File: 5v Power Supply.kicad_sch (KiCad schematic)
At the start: 15 parts, among them J15 Conn_01x02_Pin, J5 Screw_Terminal_01x02, U1 TPS56528DDA

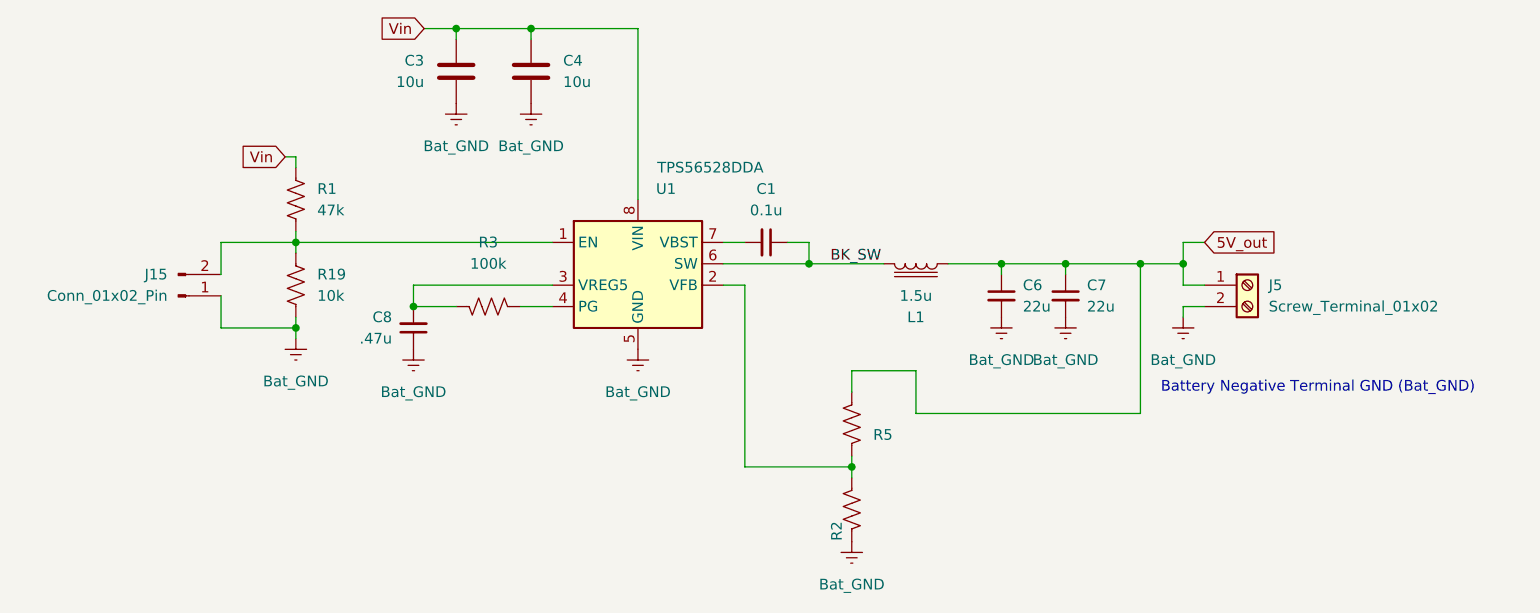
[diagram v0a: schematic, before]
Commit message: Simplified Schematic and finished PCB
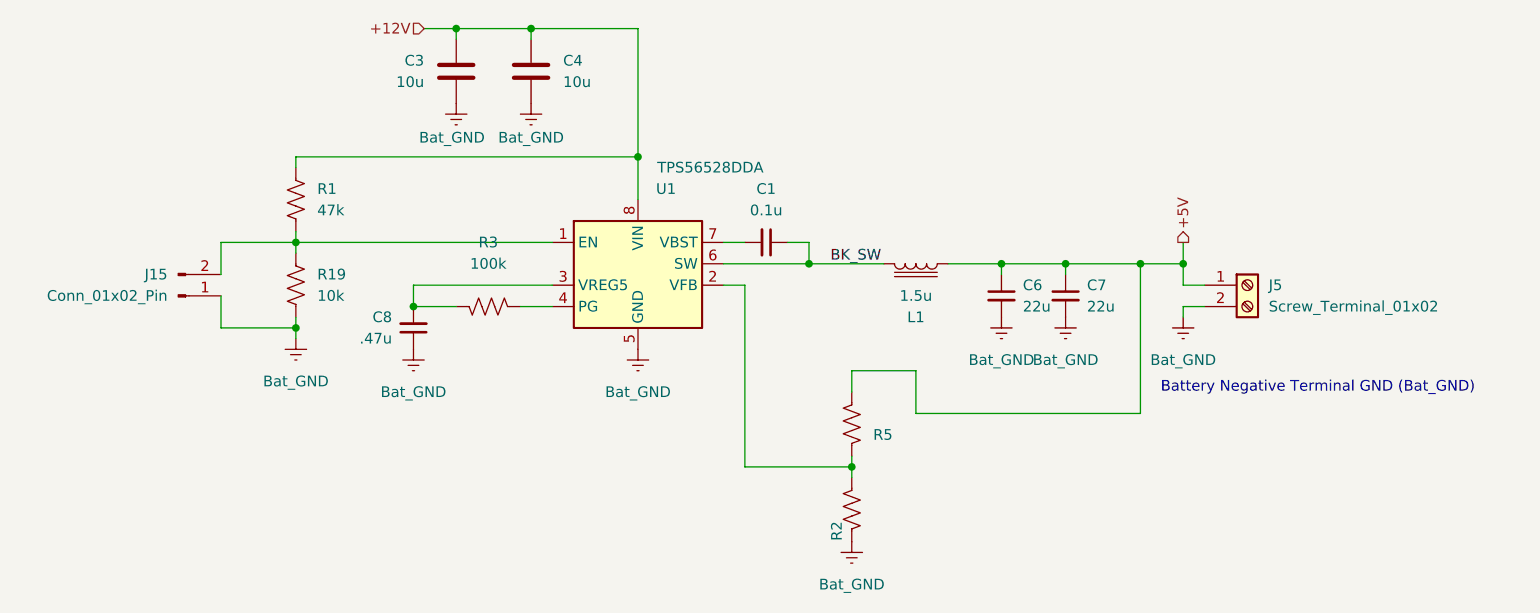
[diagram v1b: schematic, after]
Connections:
- net 5V_out renamed +5V
- net Vin renamed +12V
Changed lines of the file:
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@@
+	)
+	(junction
+		(at 140.97 77.47)
+		(diameter 0)
+		(color 0 0 0 0)
 	)
 	(junction
@@
 	(wire
 		(pts
-			(xy 140.97 82.55) (xy 140.97 62.23)
+			(xy 140.97 82.55) (xy 140.97 77.47)
 		)
 		(stroke
@@
 	(wire
 		(pts
+			(xy 140.97 77.47) (xy 140.97 62.23)
+		)
+		(stroke
+			(width 0)
+			(type default)
+		)
+	)
+	(wire
+		(pts
 			(xy 128.27 62.23) (xy 128.27 63.5)
 		)
@@
 	(wire
 		(pts
-			(xy 99.06 77.47) (xy 100.33 77.47)
-		)
-		(stroke
-			(width 0)
-			(type default)
-		)
-	)
-	(wire
-		(pts
 			(xy 166.37 114.3) (xy 153.67 114.3)
 		)
@@
 	(wire
 		(pts
-			(xy 205.74 87.63) (xy 208.28 87.63)
-		)
-		(stroke
-			(width 0)
-			(type default)
-		)
-	)
-	(wire
-		(pts
 			(xy 130.81 92.71) (xy 114.3 92.71)
 		)
@@
 		(pts
 			(xy 166.37 113.03) (xy 166.37 114.3)
+		)
+		(stroke
+			(width 0)
+			(type default)
+		)
+	)
+	(wire
+		(pts
+			(xy 100.33 77.47) (xy 140.97 77.47)
 		)
 		(stroke
@@
 		)
 	)
-	(global_label "5V_out"
+	(hierarchical_label "+12V"
 		(shape input)
-		(at 208.28 87.63 0)
-		(fields_autoplaced yes)
+		(at 115.57 62.23 180)
 		(effects
 			(font
 				(size 1.27 1.27)
 			)
-			(justify left)
-		)
-		(property "Intersheetrefs" "${INTERSHEET_REFS}"
-			(at 217.5546 87.63 0)
-			(effects
-				(font
-					(size 1.27 1.27)
-				)
-				(justify left)
-				(hide yes)
-			)
-		)
-	)
-	(global_label "Vin"
-		(shape input)
-		(at 115.57 62.23 180)
-		(fields_autoplaced yes)
+			(justify right)
+		)
+	)
+	(hierarchical_label "+5V"
+		(shape output)
+		(at 205.74 87.63 90)
 		(effects
 			(font
 				(size 1.27 1.27)
 			)
-			(justify right)
-		)
-		(property "Intersheetrefs" "${INTERSHEET_REFS}"
-			(at 109.7424 62.23 0)
-			(effects
-				(font
-					(size 1.27 1.27)
-				)
-				(justify right)
-				(hide yes)
-			)
-		)
-	)
-	(global_label "Vin"
-		(shape input)
-		(at 99.06 77.47 180)
-		(fields_autoplaced yes)
-		(effects
-			(font
-				(size 1.27 1.27)
-			)
-			(justify right)
-		)
-		(property "Intersheetrefs" "${INTERSHEET_REFS}"
-			(at 93.2324 77.47 0)
-			(effects
-				(font
-					(size 1.27 1.27)
-				)
-				(justify right)
-				(hide yes)
-			)
+			(justify left)
 		)
 	)
@@
 		)
 		(property "Value" "Bat_GND"
-			(at 128.27 76.2 0)
+			(at 128.27 75.184 0)
 			(effects
 				(font
@@
 		)
 		(property "Value" "Bat_GND"
-			(at 119.38 76.2 0)
-			(effects
-				(font
+			(at 118.872 75.184 0)
+			(effects
+				(font

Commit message: Added bypass caps for 5V output and battery to protect from in rush and back emf
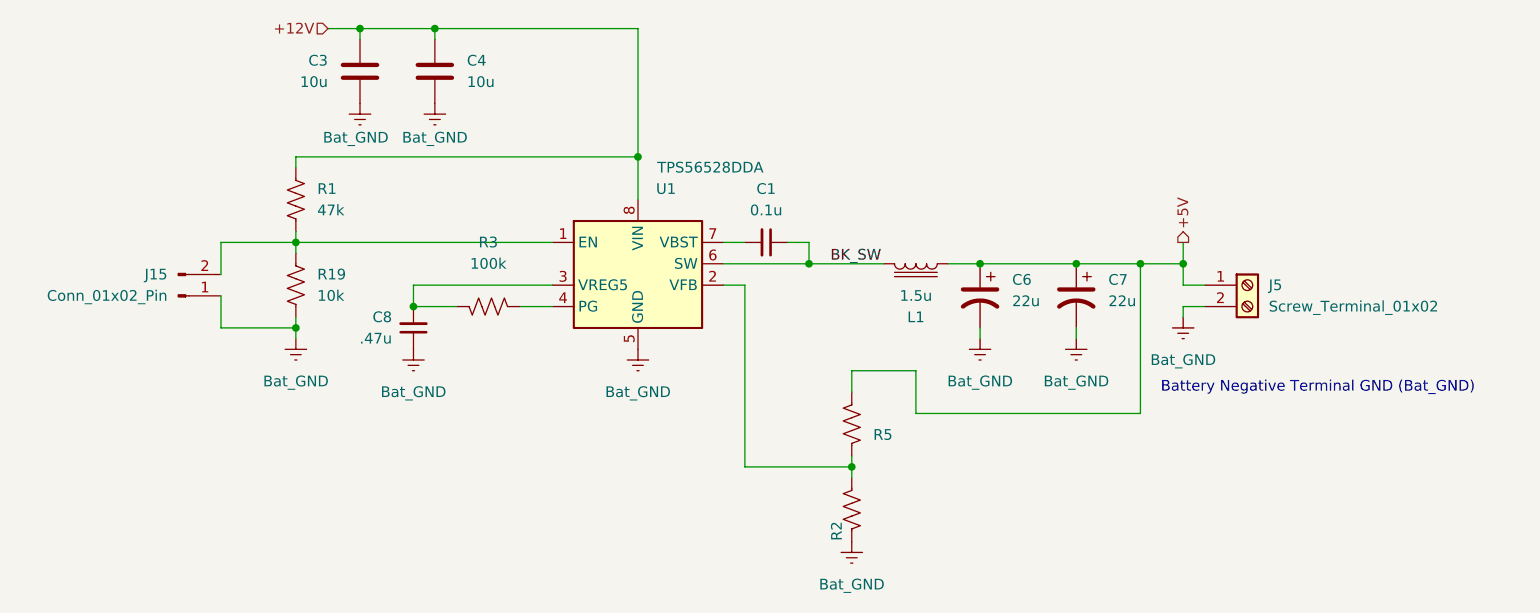
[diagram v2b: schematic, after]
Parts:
- C6, C7: footprint Capacitor_SMD:C_0805_2012Metric_Pad1.18x1.45mm_HandSolder -> Capacitor_THT:CP_Radial_D6.3mm_P2.50mm; symbol Device:C_Small -> Device:C_Polarized_US
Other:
- moved on the sheet: C3, C4
